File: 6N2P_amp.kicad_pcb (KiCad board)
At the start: 2 copper layers, 225 x 100 mm, 83 parts, among them J1 guitar_in, J2 speaker, J3 fx_send, J4 fx_return, J5 foot_sw, U1 ECC83, U2 ECC83, U3 6N1P, U4 DSN-MINI-360, U5 DSN-MINI-360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

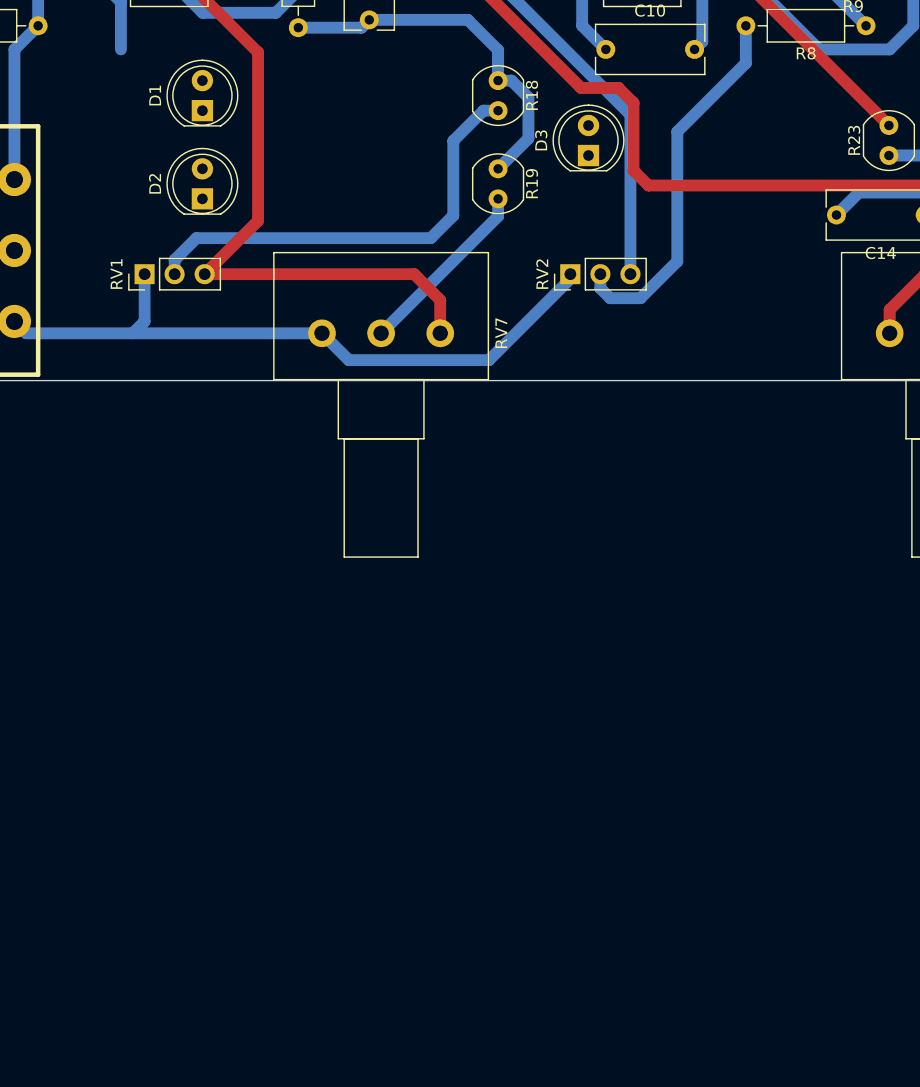
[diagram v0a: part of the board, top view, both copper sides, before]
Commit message: we have resistors now for the LEDs
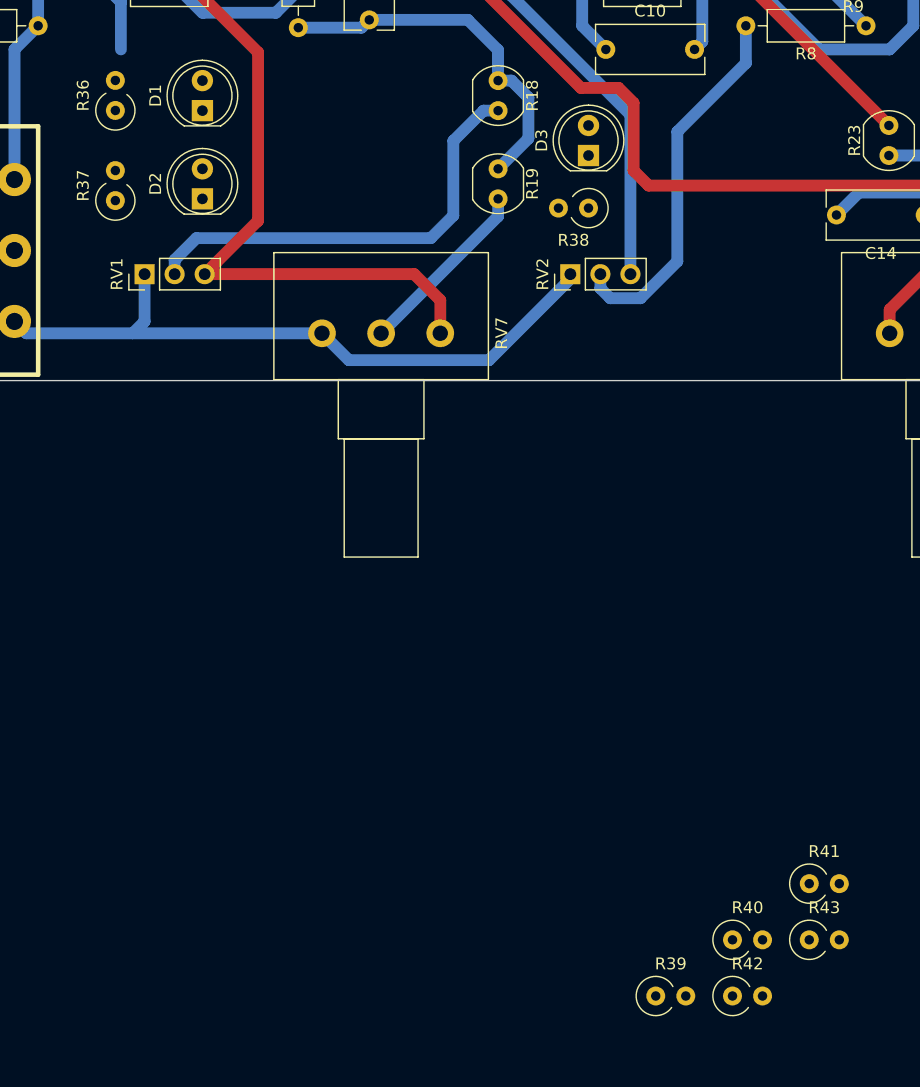
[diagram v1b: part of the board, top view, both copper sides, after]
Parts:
- added R36: 470, Resistor_THT:R_Axial_DIN0309_L9.0mm_D3.2mm_P2.54mm_Vertical, F.Cu at (49.5, 137.2)
- added R37: 470, Resistor_THT:R_Axial_DIN0309_L9.0mm_D3.2mm_P2.54mm_Vertical, F.Cu at (49.5, 144.8)
- added R38: 470, Resistor_THT:R_Axial_DIN0309_L9.0mm_D3.2mm_P2.54mm_Vertical, F.Cu at (89.5, 145.4)
- added R39: 470, Resistor_THT:R_Axial_DIN0309_L9.0mm_D3.2mm_P2.54mm_Vertical, F.Cu at (95.2, 212.0)
- added R40: 470, Resistor_THT:R_Axial_DIN0309_L9.0mm_D3.2mm_P2.54mm_Vertical, F.Cu at (101.7, 207.3)
- added R41: 470, Resistor_THT:R_Axial_DIN0309_L9.0mm_D3.2mm_P2.54mm_Vertical, F.Cu at (108.2, 202.5)
- added R42: 470, Resistor_THT:R_Axial_DIN0309_L9.0mm_D3.2mm_P2.54mm_Vertical, F.Cu at (101.7, 212.0)
- added R43: 470, Resistor_THT:R_Axial_DIN0309_L9.0mm_D3.2mm_P2.54mm_Vertical, F.Cu at (108.2, 207.3)
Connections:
- D1 pad 2: /OD -> Net-(D1-Pad2)
- D2 pad 2: /CL -> Net-(D2-Pad2)
- D3 pad 2: /OD -> Net-(D3-Pad2)
- D4 pad 2: /CL -> Net-(D4-Pad2)
- D5 pad 2: /OD -> Net-(D5-Pad2)
- D6 pad 2: /CL -> Net-(D6-Pad2)
- D7 pad 2: /OD -> Net-(D7-Pad2)
- D8 pad 2: /CL -> Net-(D8-Pad2)

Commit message: resistors and spacings
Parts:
- moved R43 145.1 mm to (240.7, 148.0), turned to 90 degrees
- moved R40 100.5 mm to (145.4, 116.8)
- moved R39 100.4 mm to (152.4, 129.5), turned to 270 degrees
- moved R42 93.3 mm to (167.0, 145.4)
- moved R41 90.8 mm to (152.4, 123.2), turned to 90 degrees
- moved RV3 19.5 mm to (164.5, 137.0)
- moved D5 17.1 mm to (175.9, 142.2)
- moved D6 16.9 mm to (234.9, 148.0)
- moved RV5 15.9 mm to (175.9, 137.0)
- moved D8 13.7 mm to (146.7, 130.2)
- moved D4 13.7 mm to (146.7, 137.2)
- moved D7 13.7 mm to (146.7, 123.0)
- moved RV4 11.3 mm to (187.3, 137.0)
- moved C11 11.3 mm to (160.0, 137.2)
- moved RV6 8.39 mm to (199.4, 137.2)
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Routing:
- net GND: track 639.2 -> 680.6 mm
- net Net-(C11-Pad2): track 15.1 -> 44.7 mm
- net Net-(R23-Pad1): track 10.7 -> 37.2 mm
- net Net-(C13-Pad1): track 18.8 -> 5.23 mm
- net Net-(RV3-Pad2): track 52.9 -> 40.5 mm
- net Net-(D8-Pad2): track 0.00 -> 10.5 mm
- net Net-(D3-Pad2): track 0.00 -> 9.15 mm
- net Net-(R21-Pad2): track 13.6 -> 5.34 mm
- net Net-(C11-Pad1): track 5.03 -> 13.1 mm
- net Net-(D2-Pad2): track 0.00 -> 7.42 mm
- net Net-(C12-Pad1): track 55.4 -> 48.0 mm
- net Net-(D1-Pad2): track 0.00 -> 7.37 mm
- net Net-(D4-Pad2): track 0.00 -> 6.77 mm
- net Net-(D5-Pad2): track 0.00 -> 6.61 mm
- net /CL: track 0.00 -> 6.35 mm
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
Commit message: more routing
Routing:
- net /CL: track 6.35 -> 237.7 mm, vias 0 -> 1
- net /OD: track 0.00 -> 176.5 mm, vias 0 -> 1
- net Net-(R18-Pad2): track 37.5 -> 48.7 mm
- net /clean_channel_bypass: track 119.7 -> 115.3 mm
- net Net-(C3-Pad2): track 33.5 -> 33.0 mm

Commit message: everything routed. woah!
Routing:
- net GND: track 680.2 -> 890.3 mm, vias 0 -> 1
- net /CL: track 237.7 -> 236.4 mm
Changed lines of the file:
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@@
     (thickness 1.6)
     (drawings 11)
-    (tracks 578)
+    (tracks 606)
     (zones 0)
     (modules 91)
@@
   (segment (start 36.99796 154.99948) (end 24.999 143.00052) (width 1) (layer B.Cu) (net 2))
   (segment (start 40.99846 154.99948) (end 36.99796 154.99948) (width 1) (layer B.Cu) (net 2))
-  (segment (start 139 156) (end 136 156) (width 1) (layer B.Cu) (net 2))
-  (segment (start 136 156) (end 131 151) (width 1) (layer B.Cu) (net 2))
-  (segment (start 131 151) (end 131 139) (width 1) (layer B.Cu) (net 2))
   (segment (start 194.5 118.25) (end 190.75 118.25) (width 1) (layer F.Cu) (net 2))
   (segment (start 190.75 118.25) (end 183 126) (width 1) (layer F.Cu) (net 2))
@@
   (segment (start 67 156) (end 69.270001 158.270001) (width 1) (layer B.Cu) (net 2))
   (segment (start 88 151.395) (end 88 151) (width 1) (layer B.Cu) (net 2))
-  (segment (start 81.124999 158.270001) (end 88 151.395) (width 1) (layer B.Cu) (net 2))
   (segment (start 156.18 141) (end 150.525 141) (width 1) (layer B.Cu) (net 2))
   (segment (start 156.18 141) (end 151 141) (width 1) (layer B.Cu) (net 2))
@@
   (segment (start 64.512002 124.46) (end 73.852002 124.46) (width 1) (layer B.Cu) (net 2))
   (segment (start 78.5 114.25) (end 78.5 119.14) (width 1) (layer B.Cu) (net 2))
+  (segment (start 156 128) (end 155 127) (width 1) (layer F.Cu) (net 2))
+  (segment (start 147.105002 130.175) (end 146.685 130.175) (width 1) (layer F.Cu) (net 2))
+  (segment (start 150.280002 127) (end 147.105002 130.175) (width 1) (layer F.Cu) (net 2))
+  (segment (start 155 127) (end 150.280002 127) (width 1) (layer F.Cu) (net 2))
+  (segment (start 89.535 140.97) (end 91.44 142.875) (width 1) (layer B.Cu) (net 2))
+  (segment (start 91.44 142.875) (end 91.44 147.32) (width 1) (layer B.Cu) (net 2))
+  (segment (start 88 150.76) (end 88 151) (width 1) (layer B.Cu) (net 2))
+  (segment (start 91.44 147.32) (end 88 150.76) (width 1) (layer B.Cu) (net 2))
+  (segment (start 98.5 132) (end 98.5 133.91) (width 1) (layer B.Cu) (net 2))
+  (segment (start 98.5 133.91) (end 95.25 137.16) (width 1) (layer B.Cu) (net 2))
+  (segment (start 95.25 137.16) (end 95.25 141.605) (width 1) (layer B.Cu) (net 2))
+  (via (at 95.25 141.605) (size 1) (drill 0.6) (layers F.Cu B.Cu) (net 2))
+  (segment (start 90.17 141.605) (end 89.535 140.97) (width 1) (layer F.Cu) (net 2))
+  (segment (start 95.25 141.605) (end 90.17 141.605) (width 1) (layer F.Cu) (net 2))
+  (segment (start 56.89 137.175) (end 55.865 137.175) (width 1) (layer B.Cu) (net 2))
+  (segment (start 55.865 137.175) (end 52.705 140.335) (width 1) (layer B.Cu) (net 2))
+  (segment (start 48.622998 140.335) (end 45.72 143.237998) (width 1) (layer B.Cu) (net 2))
+  (segment (start 52.705 140.335) (end 48.622998 140.335) (width 1) (layer B.Cu) (net 2))
+  (segment (start 45.72 150.27794) (end 40.99846 154.99948) (width 1) (layer B.Cu) (net 2))
+  (segment (start 45.72 143.237998) (end 45.72 150.27794) (width 1) (layer B.Cu) (net 2))
+  (segment (start 139 156) (end 131.655 156) (width 1) (layer B.Cu) (net 2))
+  (segment (start 89.690001 158.270001) (end 85.4075 153.9875) (width 1) (layer B.Cu) (net 2))
+  (segment (start 129.384999 158.270001) (end 89.690001 158.270001) (width 1) (layer B.Cu) (net 2))
+  (segment (start 131.655 156) (end 129.384999 158.270001) (width 1) (layer B.Cu) (net 2))
+  (segment (start 81.124999 158.270001) (end 85.4075 153.9875) (width 1) (layer B.Cu) (net 2))
+  (segment (start 85.4075 153.9875) (end 88 151.395) (width 1) (layer B.Cu) (net 2))
+  (segment (start 184.729999 158.270001) (end 187 156) (width 1) (layer B.Cu) (net 2))
+  (segment (start 141.270001 158.270001) (end 184.729999 158.270001) (width 1) (layer B.Cu) (net 2))
+  (segment (start 139 156) (end 141.270001 158.270001) (width 1) (layer B.Cu) (net 2))
+  (segment (start 224.679999 158.270001) (end 234.95 148) (width 1) (layer B.Cu) (net 2))
+  (segment (start 189.270001 158.270001) (end 224.679999 158.270001) (width 1) (layer B.Cu) (net 2))
+  (segment (start 187 156) (end 189.270001 158.270001) (width 1) (layer B.Cu) (net 2))
+  (segment (start 175.895 137) (end 175.895 142.24) (width 1) (layer B.Cu) (net 2))
   (segment (start 34 117) (end 35 116) (width 1) (layer B.Cu) (net 5))
   (segment (start 30 117) (end 34 117) (width 1) (layer B.Cu) (net 5))
@@
   (segment (start 74.295 139.7) (end 66.675 147.32) (width 1) (layer B.Cu) (net 67))
   (segment (start 51.435 144.78) (end 49.53 144.78) (width 1) (layer B.Cu) (net 67))
-  (segment (start 75.565 139.7) (end 74.295 139.7) (width 1) (layer B.Cu) (net 67))
   (via (at 74.93 139.7) (size 1) (drill 0.6) (layers F.Cu B.Cu) (net 67))
   (segment (start 74.295 139.7) (end 74.93 139.7) (width 1) (layer B.Cu) (net 67))

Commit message: pdf of schematic
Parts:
- moved R43 20.1 mm to (221.4, 153.5), turned to 0 degrees
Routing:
- net GND: track 890.3 -> 1047.3 mm
- net /fx_return: track 69.5 -> 43.1 mm
- net Net-(D6-Pad2): track 5.73 -> 23.2 mm
- net /CL: track 236.4 -> 223.2 mm
- net /HV_in: track 216.2 -> 212.0 mm
